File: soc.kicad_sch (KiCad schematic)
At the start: 89 parts, among them U1 MPFS250T-FCVG484

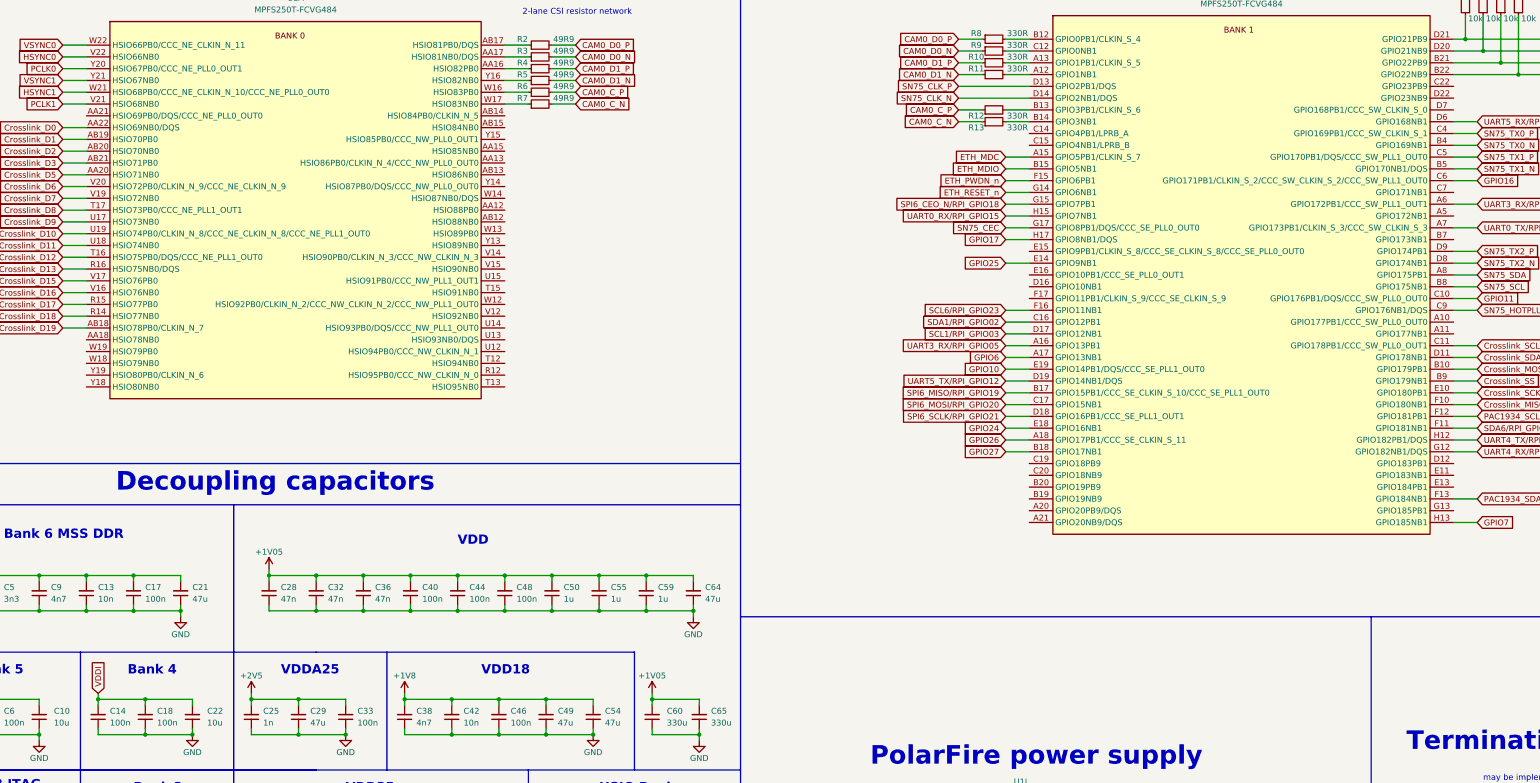
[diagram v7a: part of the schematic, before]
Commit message: [#54899] Flag not connected pins
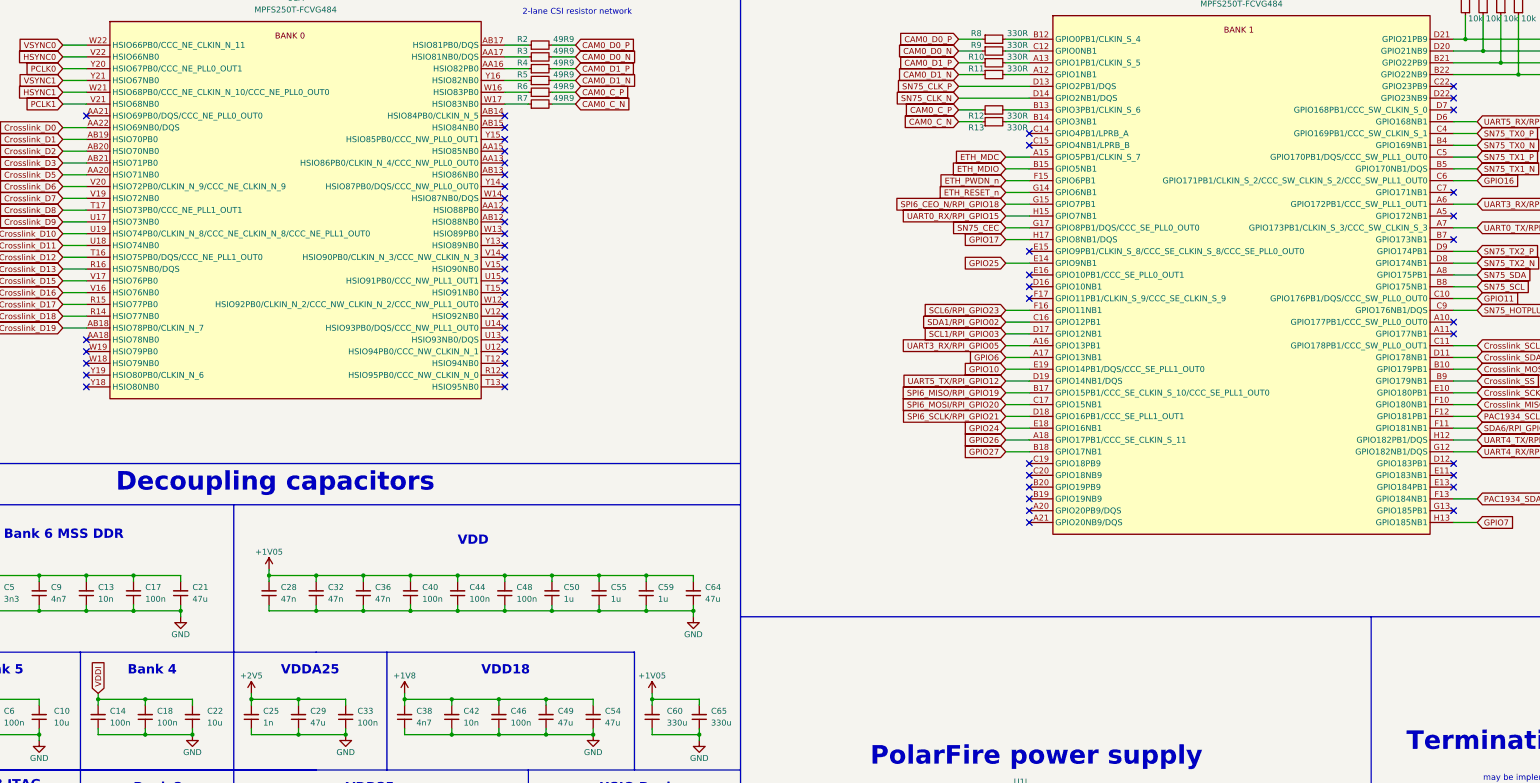
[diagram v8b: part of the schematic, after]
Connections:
- net +1V8: now also C54.2
- no-connect marks 0 -> 54
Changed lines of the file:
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@@
   (junction (at 172.72 240.03) (diameter 0) (color 0 0 0 0)
   )
+  (junction (at 63.5 196.85) (diameter 0) (color 0 0 0 0)
+  )
+  (junction (at 182.88 276.86) (diameter 0) (color 0 0 0 0)
+  )
+  (junction (at 182.88 223.52) (diameter 0) (color 0 0 0 0)
+  )
+  (junction (at 30.48 223.52) (diameter 0) (color 0 0 0 0)
+  )
+  (junction (at 30.48 162.56) (diameter 0) (color 0 0 0 0)
+  )
   (junction (at 149.86 189.23) (diameter 0) (color 0 0 0 0)
   )
-  (junction (at 63.5 196.85) (diameter 0) (color 0 0 0 0)
-  )
-  (junction (at 182.88 276.86) (diameter 0) (color 0 0 0 0)
-  )
-  (junction (at 182.88 223.52) (diameter 0) (color 0 0 0 0)
-  )
-  (junction (at 30.48 223.52) (diameter 0) (color 0 0 0 0)
-  )
-  (junction (at 30.48 162.56) (diameter 0) (color 0 0 0 0)
-  )
   (junction (at 162.56 269.24) (diameter 0) (color 0 0 0 0)
   )
@@
   (junction (at 109.22 240.03) (diameter 0) (color 0 0 0 0)
   )
+  (no_connect (at 345.44 140.97))
+  (no_connect (at 345.44 57.15))
+  (no_connect (at 254 143.51))
+  (no_connect (at 50.8 63.5))
+  (no_connect (at 50.8 119.38))
+  (no_connect (at 345.44 107.95))
+  (no_connect (at 254 69.85))
+  (no_connect (at 140.97 104.14))
+  (no_connect (at 140.97 63.5))
+  (no_connect (at 345.44 110.49))
+  (no_connect (at 140.97 114.3))
+  (no_connect (at 345.44 143.51))
+  (no_connect (at 140.97 106.68))
+  (no_connect (at 140.97 81.28))
+  (no_connect (at 50.8 114.3))
+  (no_connect (at 140.97 91.44))
+  (no_connect (at 345.44 80.01))
+  (no_connect (at 345.44 59.69))
+  (no_connect (at 140.97 93.98))
+  (no_connect (at 140.97 66.04))
+  (no_connect (at 345.44 90.17))
+  (no_connect (at 140.97 121.92))
+  (no_connect (at 254 151.13))
+  (no_connect (at 254 67.31))
+  (no_connect (at 140.97 88.9))
+  (no_connect (at 140.97 101.6))
+  (no_connect (at 254 100.33))
+  (no_connect (at 345.44 62.23))
+  (no_connect (at 140.97 119.38))
+  (no_connect (at 140.97 116.84))
+  (no_connect (at 140.97 96.52))
+  (no_connect (at 345.44 85.09))
+  (no_connect (at 140.97 109.22))
+  (no_connect (at 140.97 68.58))
+  (no_connect (at 140.97 83.82))
+  (no_connect (at 254 148.59))
+  (no_connect (at 50.8 121.92))
+  (no_connect (at 254 146.05))
+  (no_connect (at 140.97 86.36))
+  (no_connect (at 254 102.87))
+  (no_connect (at 254 92.71))
+  (no_connect (at 345.44 138.43))
+  (no_connect (at 345.44 148.59))
+  (no_connect (at 140.97 99.06))
+  (no_connect (at 140.97 78.74))
+  (no_connect (at 254 140.97))
+  (no_connect (at 50.8 111.76))
+  (no_connect (at 254 138.43))
+  (no_connect (at 254 97.79))
+  (no_connect (at 140.97 111.76))
+  (no_connect (at 50.8 116.84))
+  (no_connect (at 140.97 73.66))
+  (no_connect (at 140.97 76.2))
+  (no_connect (at 140.97 71.12))
   (wire (pts (xy 160.02 195.58) (xy 160.02 196.85))
     (stroke (width 0) (type default))
@@
     (stroke (width 0) (type default))
   )
-  (wire (pts (xy 149.86 189.23) (xy 159.914 189.23))
-    (stroke (width 0) (type default))
-  )
   (wire (pts (xy 120.65 170.18) (xy 130.81 170.18))
     (stroke (width 0) (type default))
@@
     (stroke (width 0) (type default))
   )
+  (wire (pts (xy 160.02 189.23) (xy 160.02 190.5))
+    (stroke (width 0) (type default))
+  )
   (wire (pts (xy 30.48 170.18) (xy 40.64 170.18))
     (stroke (width 0) (type default))
@@
     (stroke (width 0) (type default))
   )
-  (wire (pts (xy 160.02 189.23) (xy 160.02 190.5))
-    (stroke (width 0) (type default))
-  )
   (wire (pts (xy 248.92 85.09) (xy 254 85.09))
     (stroke (width 0) (type default))
@@
     (stroke (width 0) (type default))
   )
+  (wire (pts (xy 149.86 189.23) (xy 160.02 189.23))
+    (stroke (width 0) (type default))
+  )
